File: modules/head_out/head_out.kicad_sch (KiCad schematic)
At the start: 33 parts, among them J1 AudioJack3, U1 MCP6002-xSN

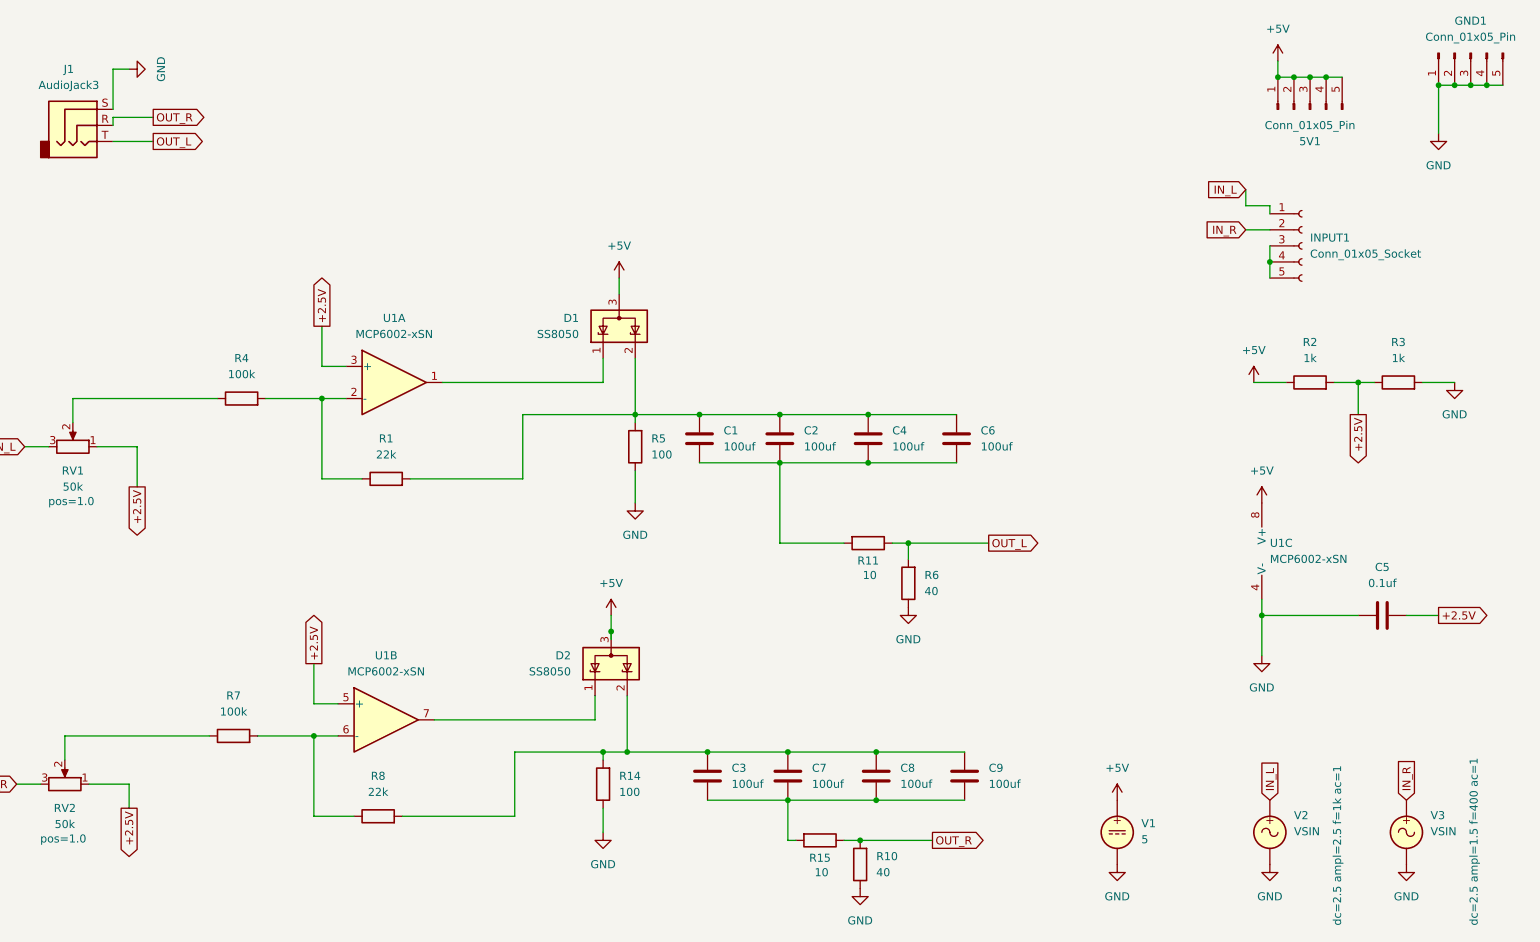
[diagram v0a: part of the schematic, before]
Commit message: head_out: Add more volume to support larger headphones. Now we offer more volume and removed the transistor. The opamp can handle the power requirment decently.
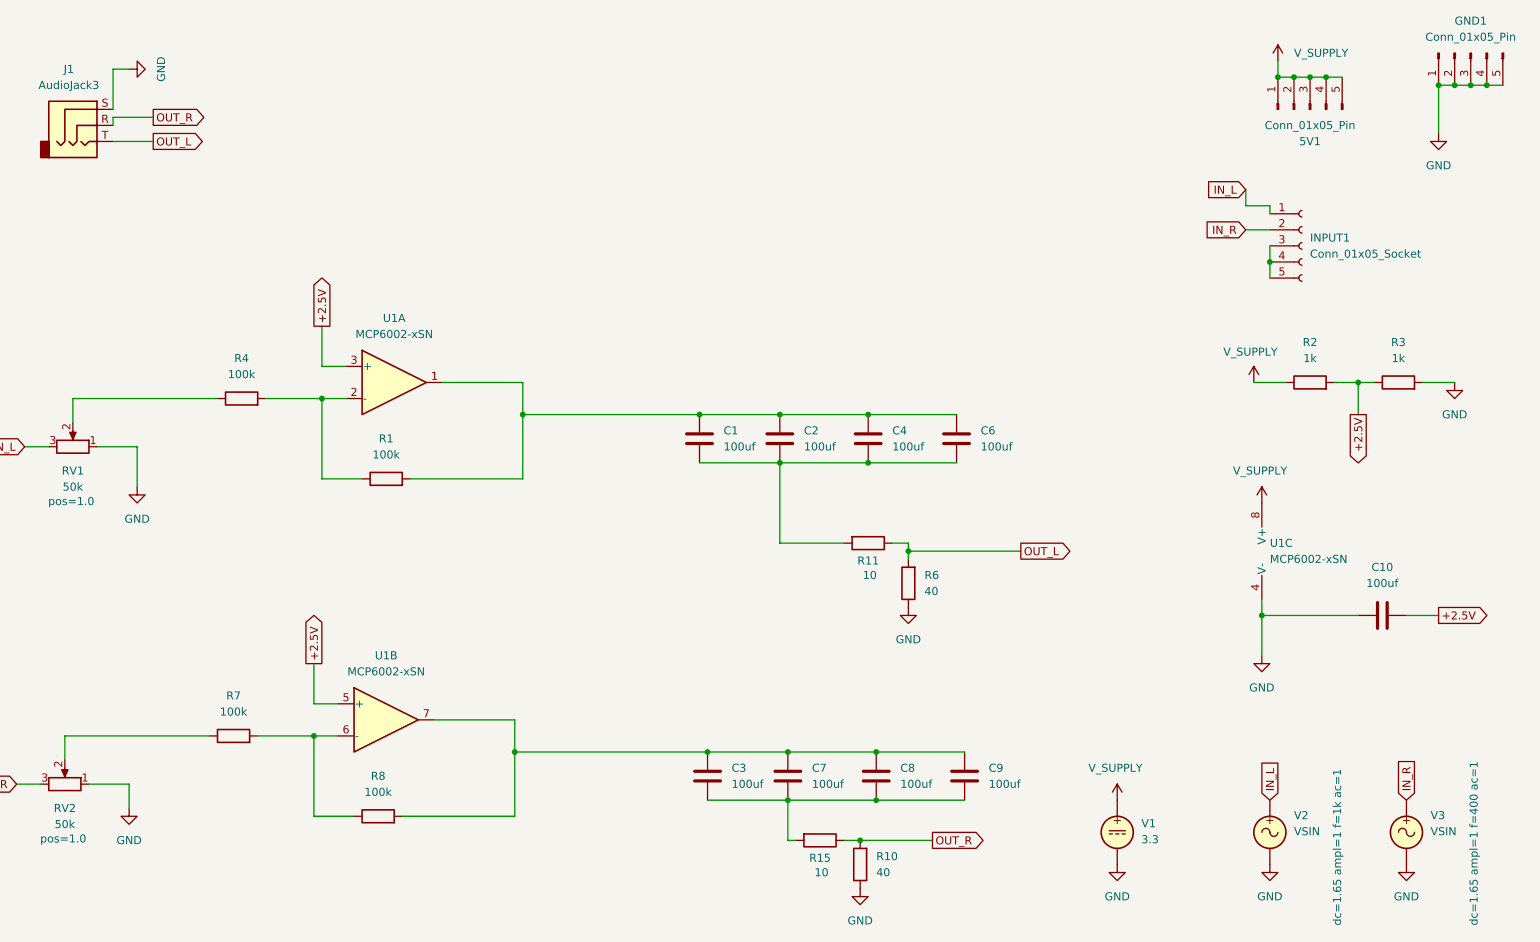
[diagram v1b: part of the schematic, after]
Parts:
- removed C5: 0.1uf, Capacitor_SMD:C_0402_1005Metric, symbol Device:C
- removed D1, D2: SS8050, Package_TO_SOT_SMD:SOT-23, symbol Power_Protection:ESDA5V3L
- removed R14, R5: 100, Resistor_SMD:R_1206_3216Metric, symbol Device:R
- added C10: 100uf, Capacitor_SMD:C_1206_3216Metric, symbol Device:C
- R1, R8: value 22k -> 100k
- V1: value 5 -> 3.3
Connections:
- net +2.5V: now also C10.2; no longer RV1.1, RV2.1
- net GND: now also RV1.1, RV2.1, C10.1
- net at C3.1, C7.1, C8.1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: now also U1.7
- net at C1.1, C2.1, C4.1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: now also U1.1
- net +5V renamed V_SUPPLY

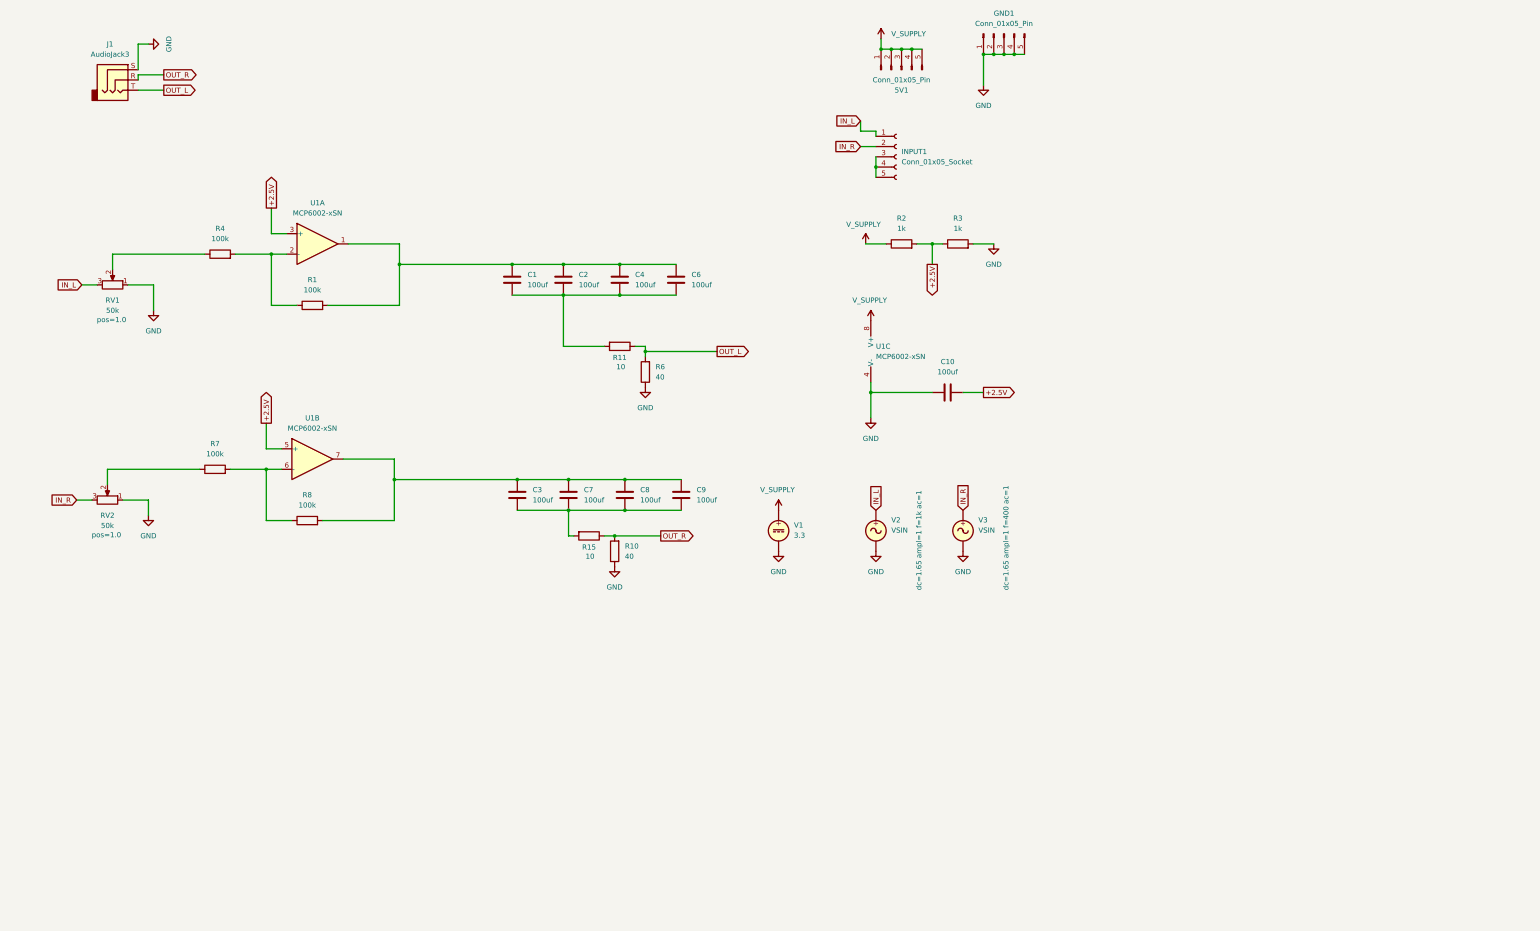
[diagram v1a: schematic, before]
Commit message: head_out: Add left to right input normalling This is a passive implementation and it works pretty well.
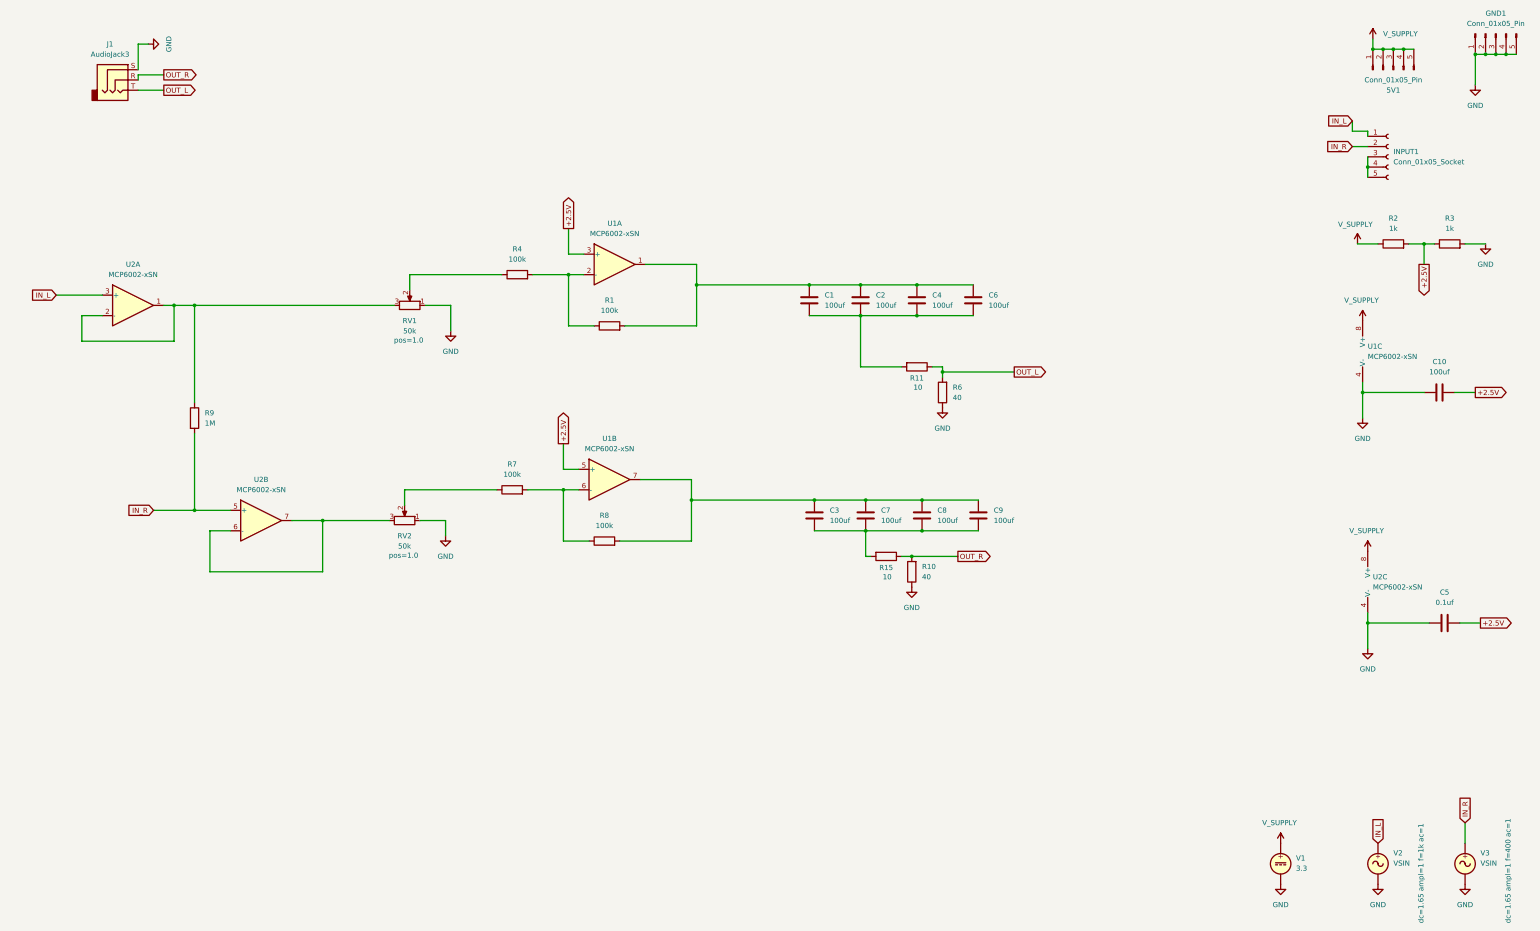
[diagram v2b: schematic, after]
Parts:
- added C5: 0.1uf, Capacitor_SMD:C_0402_1005Metric, symbol Device:C
- added R9: 1M, Resistor_SMD:R_0402_1005Metric, symbol Device:R
- added U2: MCP6002-xSN, Package_SO:SOIC-8-1EP_3.9x4.9mm_P1.27mm_EP2.29x3mm, symbol Amplifier_Operational:MCP6002-xSN
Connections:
- net +2.5V: now also C5.2
- net GND: now also C5.1, U2.4 (V-)
- net IN_L: now also U2.3 (+); no longer RV1.3
- net IN_R: now also R9.2, U2.5 (+); no longer RV2.3
- net V_SUPPLY: now also U2.8 (V+)
- new net: R9.1, RV1.3, U2.1, U2.2 (-)
- new net: RV2.3, U2.6 (-), U2.7
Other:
- moved on the sheet: 5V1, C1, C10, C2, C3, C4, C6, C7, C8, C9, GND1, INPUT1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

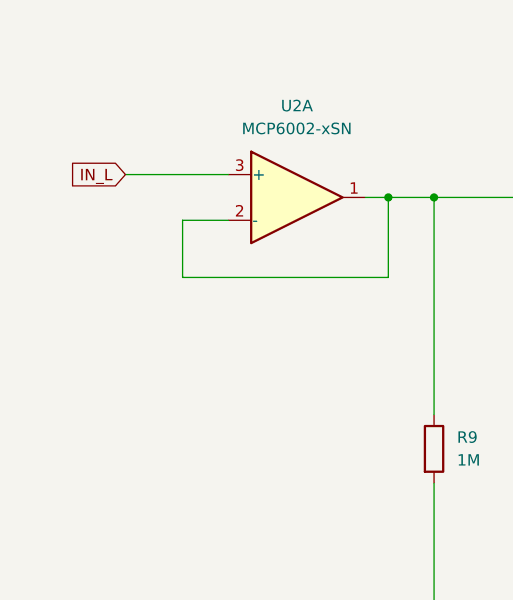
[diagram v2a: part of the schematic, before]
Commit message: head_out: Add input normalizing
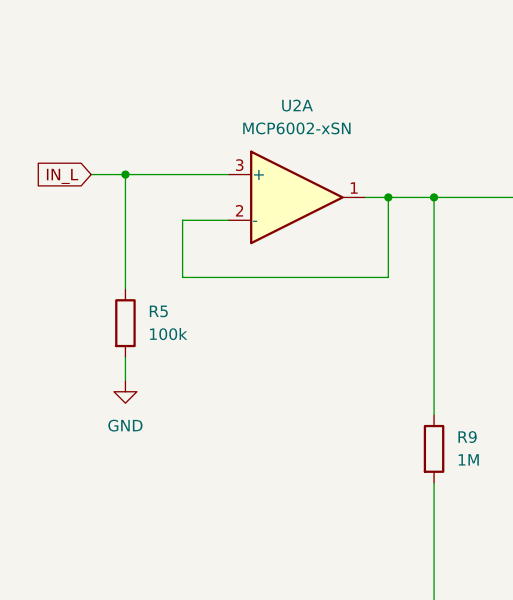
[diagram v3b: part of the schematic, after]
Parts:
- added R5: 100k, Resistor_SMD:R_0402_1005Metric, symbol Device:R
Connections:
- net GND: now also R5.2
- net IN_L: now also R5.1
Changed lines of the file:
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@@
 	)
 	(junction
+		(at 29.21 90.17)
+		(diameter 0)
+		(color 0 0 0 0)
+	)
+	(junction
 		(at 215.9 87.63)
 		(diameter 0)
@@
 	(wire
 		(pts
+			(xy 29.21 113.03) (xy 29.21 110.49)
+		)
+		(stroke
+			(width 0)
+			(type default)
+		)
+	)
+	(wire
+		(pts
 			(xy 353.06 114.3) (xy 368.3 114.3)
 		)
@@
 	(wire
 		(pts
-			(xy 29.21 90.17) (xy 40.64 90.17)
+			(xy 25.4 90.17) (xy 29.21 90.17)
 		)
 		(stroke
@@
 	(wire
 		(pts
+			(xy 29.21 90.17) (xy 40.64 90.17)
+		)
+		(stroke
+			(width 0)
+			(type default)
+		)
+	)
+	(wire
+		(pts
 			(xy 168.91 151.13) (xy 186.69 151.13)
 		)
@@
 		)
 	)
+	(wire
+		(pts
+			(xy 29.21 102.87) (xy 29.21 90.17)
+		)
+		(stroke
+			(width 0)
+			(type default)
+		)
+	)
 	(global_label "+2.5V"
 		(shape output)
@@
 	(global_label "IN_L"
 		(shape input)
-		(at 29.21 90.17 180)
+		(at 25.4 90.17 180)
 		(fields_autoplaced yes)
 		(effects
@@
 		)
 		(property "Intersheetrefs" "${INTERSHEET_REFS}"
-			(at 22.2938 90.17 0)
+			(at 18.4838 90.17 0)
 			(effects
 				(font
@@
 	(symbol
 		(lib_id "power:GND")
+		(at 29.21 113.03 0)
+		(unit 1)
+		(exclude_from_sim no)
+		(in_bom yes)
+		(on_board yes)
+		(dnp no)
+		(property "Reference" "#PWR015"
+			(at 29.21 119.38 0)
+			(effects
+				(font
+					(size 1.27 1.27)
+				)
+				(hide yes)
+			)
+		)
+		(property "Value" "GND"
+			(at 29.21 118.11 0)
+			(effects
+				(font
+					(size 1.27 1.27)
+				)
+			)
+		)
+		(property "Footprint" ""
+			(at 29.21 113.03 0)
+			(effects
+				(font
+					(size 1.27 1.27)
+				)
+				(hide yes)
+			)
+		)
+		(property "Datasheet" ""
+			(at 29.21 113.03 0)
+			(effects
+				(font
+					(size 1.27 1.27)
+				)
+				(hide yes)
+			)
+		)
+		(property "Description" "Power symbol creates a global label with name \"GND\" , ground"
+			(at 29.21 113.03 0)
+			(effects
+				(font
+					(size 1.27 1.27)
+				)
+				(hide yes)
+			)
+		)
+		(pin "1"
+		)
+		(instances
+			(project "head_out"
+				(path "/b63493d3-5f6d-47e3-845b-87e7090fc1ab"
+					(reference "#PWR015")
+					(unit 1)
+				)
+			)
+		)
+	)
+	(symbol
+		(lib_id "power:GND")
 		(at 332.74 236.22 0)
 		(unit 1)
@@
 					(unit 1)
 				)
+			)
+		)
+	)
+	(symbol
+		(lib_id "Device:R")
+		(at 29.21 106.68 0)
+		(unit 1)
+		(exclude_from_sim no)
+		(in_bom yes)
+		(on_board yes)
+		(dnp no)
+		(fields_autoplaced yes)
+		(property "Reference" "R5"
+			(at 31.75 105.4099 0)
+			(effects
+				(font
+					(size 1.27 1.27)
+				)
+				(justify left)
+			)
+		)
+		(property "Value" "100k"
+			(at 31.75 107.9499 0)
+			(effects
+				(font
+					(size 1.27 1.27)
+				)
+				(justify left)
+			)
+		)
+		(property "Footprint" "Resistor_SMD:R_0402_1005Metric"
+			(at 27.432 106.68 90)
+			(effects
+				(font
+					(size 1.27 1.27)
+				)
+				(hide yes)
+			)
+		)
+		(property "Datasheet" "~"
+			(at 29.21 106.68 0)
+			(effects
+				(font
+					(size 1.27 1.27)
+				)
+				(hide yes)
+			)
+		)
+		(property "Description" "Resistor"
+			(at 29.21 106.68 0)
+			(effects
+				(font
+					(size 1.27 1.27)
+				)
+				(hide yes)
+			)
+		)
+		(pin "2"
+		)
+		(pin "1"
+		)
+		(instances
+			(project "head_out"
+				(path "/b63493d3-5f6d-47e3-845b-87e7090fc1ab"
+					(reference "R5")
+					(unit 1)
+				)
